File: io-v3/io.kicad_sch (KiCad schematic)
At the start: 99 parts, among them P1 OUT_GND, P10 INJ-CPU, P11 INJECTORS, P12 LSD-CPU, P13 LSDS, P2 TRIG-cpu, P3 DIG-CPU, P4 IN-CPU, P5 CPU_PWR, P6 TRIG-IN, P7 DIG-IN, P8 IGNITION, P9 PWR_IN, Q1 MOSFET, Q2 MOSFET, Q3 MOSFET, Q4 MOSFET, Q5 MOSFET, Q6 MOSFET, Q7 MOSFET, Q8 MOSFET, U1 LM2940, U12 MIC4469, U13 MIC4469, U2 MIC4469, U3 MAX9926UAEE+

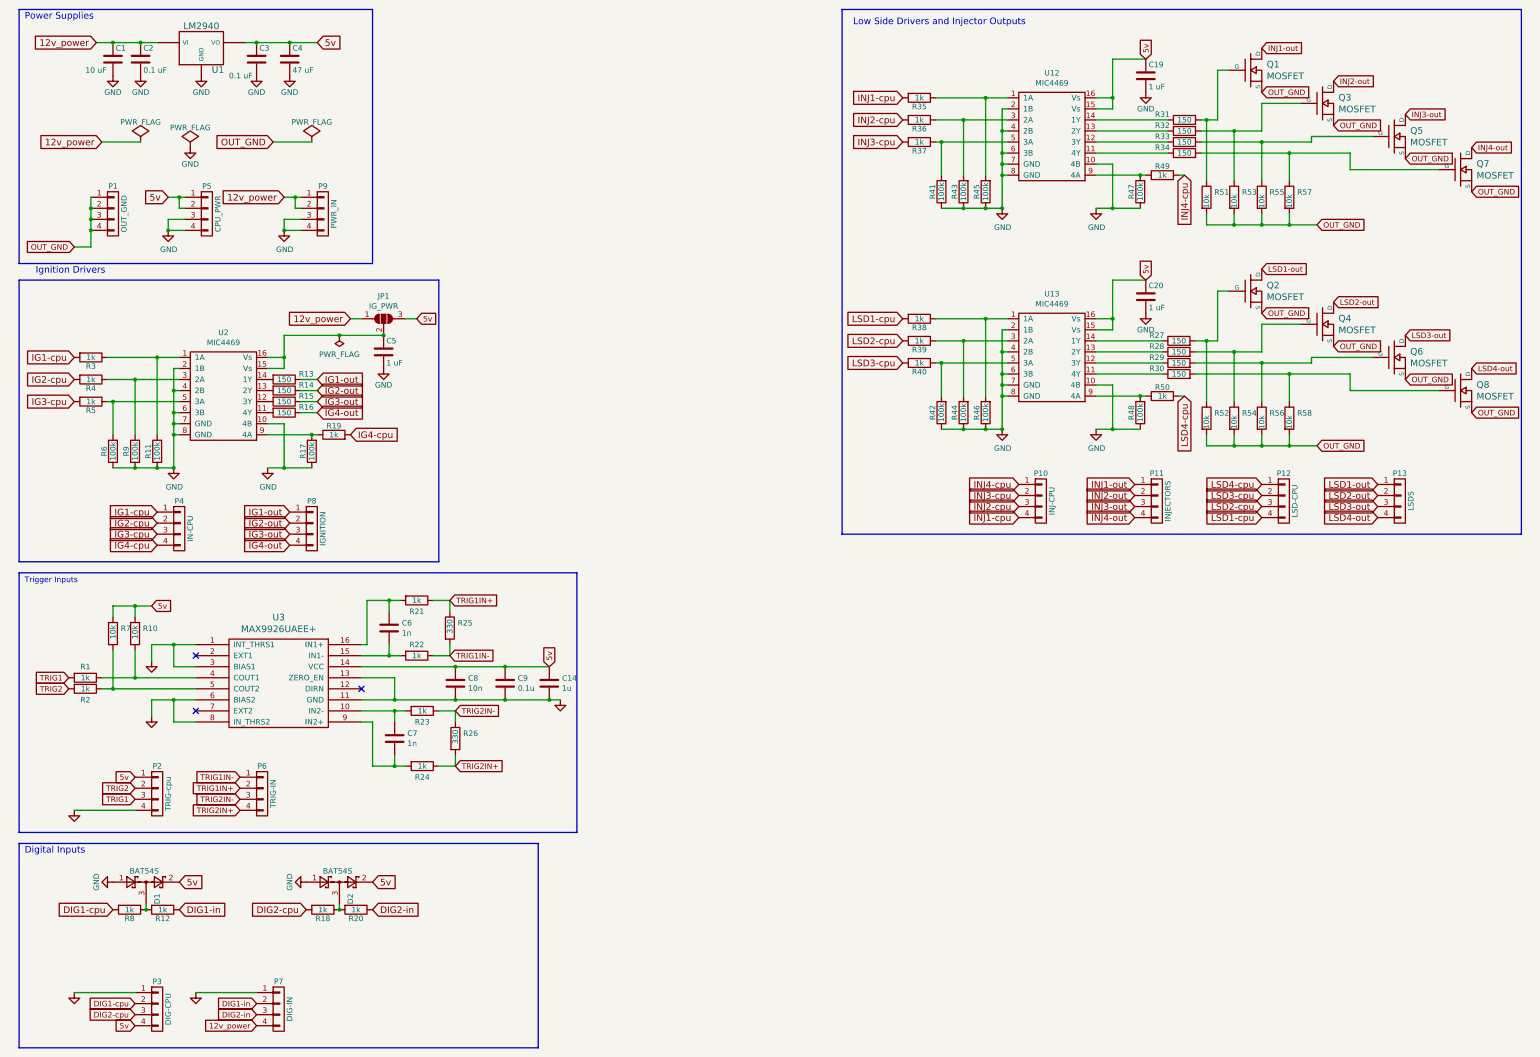
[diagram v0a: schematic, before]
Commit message: Add LEDs and make a board size
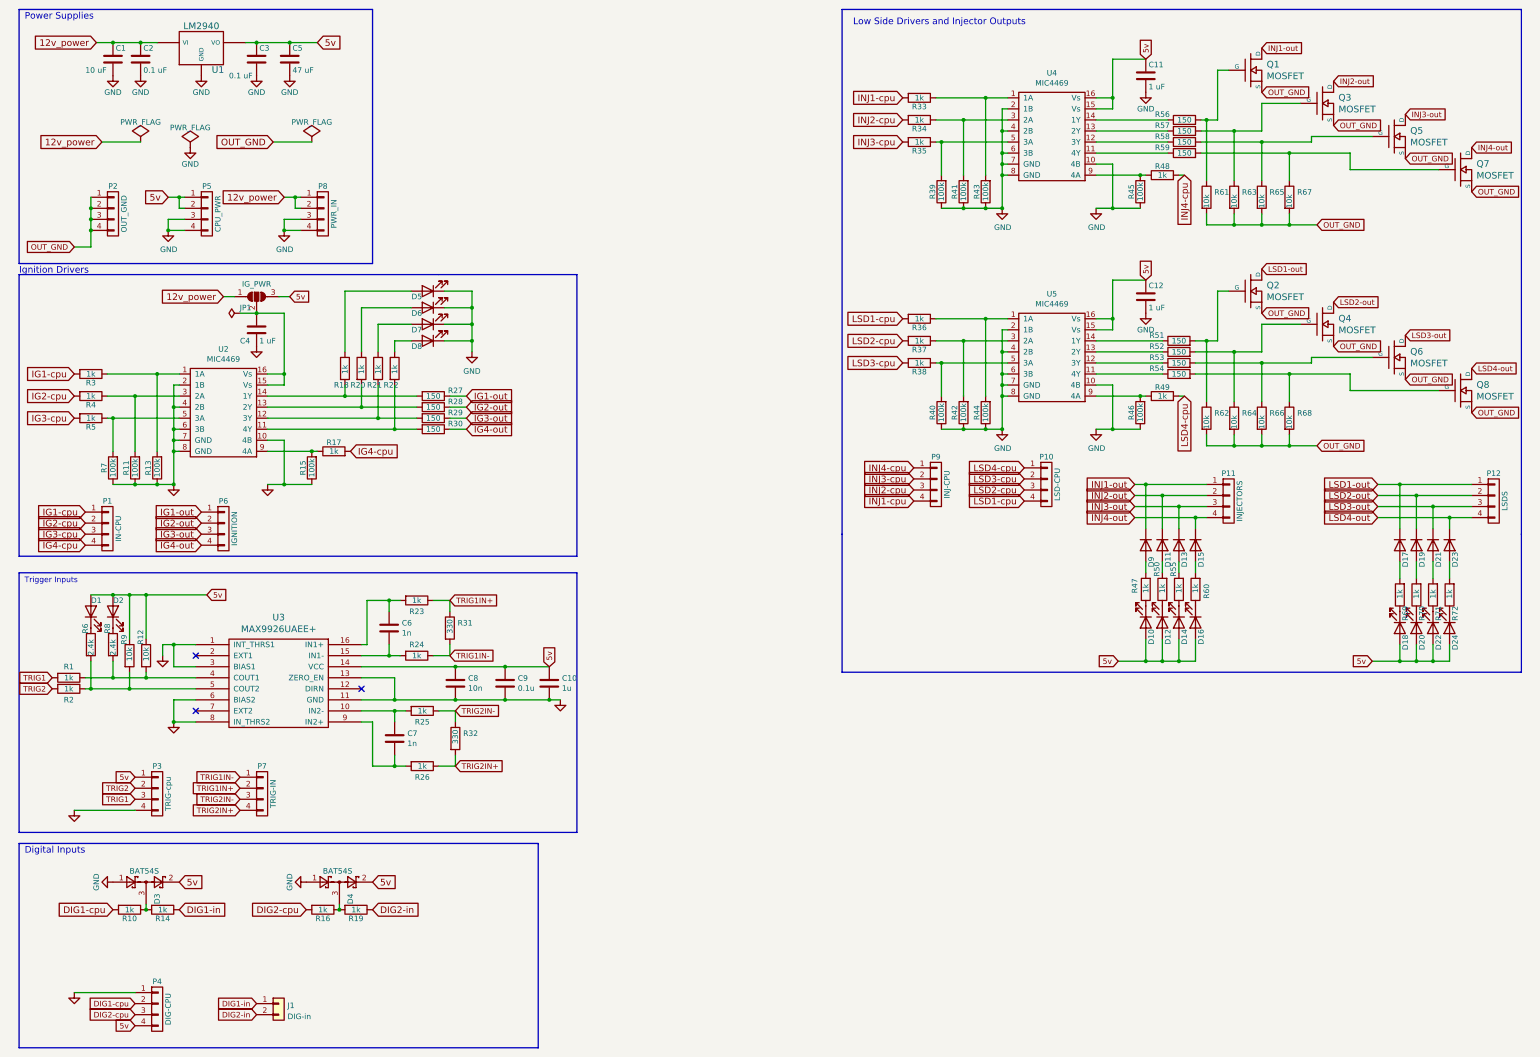
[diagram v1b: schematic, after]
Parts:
- removed P7: DIG-IN, Connector_PinHeader_2.54mm:PinHeader_1x04_P2.54mm_Vertical, symbol io-rescue:CONN_01X04-io-rescue-io-rescue
- added D1, D10, D12, D14, D16, D18, D2, D20, D22, D24, D5, D6, D7, D8: LED, LED_SMD:LED_0805_2012Metric_Pad1.15x1.40mm_HandSolder, symbol Device:LED
- added D11, D13, D15, D17, D19, D21, D23, D9: 1N4148, Diode_SMD:D_0805_2012Metric_Pad1.15x1.40mm_HandSolder, symbol Diode:1N4148
- added J1: DIG-in, Connector_PinHeader_2.54mm:PinHeader_1x02_P2.54mm_Vertical, symbol Connector_Generic:Conn_01x02
- added R18, R20, R21, R22, R47, R50, R55, R60, R69, R70, R71, R72: 1k, Resistor_SMD:R_0805_2012Metric_Pad1.20x1.40mm_HandSolder, symbol Device:R
- added R6, R8: 2.4k, Resistor_SMD:R_0805_2012Metric_Pad1.20x1.40mm_HandSolder, symbol Device:R
- renumbered C14 to C10, C19 to C11, C20 to C12, C5 to C4, C4 to C5, D1 to D3, D2 to D4, P4 to P1, P12 to P10, P13 to P12, P1 to P2, P2 to P3, P3 to P4, P8 to P6, P6 to P7, P9 to P8, P10 to P9, R8 to R10, R9 to R11, R10 to R12, R11 to R13, R12 to R14, R17 to R15, R18 to R16, R19 to R17, R20 to R19, R21 to R23, R22 to R24, R23 to R25, R24 to R26, R13 to R27, R14 to R28, R15 to R29, R16 to R30, R25 to R31, R26 to R32, R35 to R33, R36 to R34, R37 to R35, R38 to R36, R39 to R37, R40 to R38, R41 to R39, R42 to R40, R43 to R41, R44 to R42, R45 to R43, R46 to R44, R47 to R45, R48 to R46, R49 to R48, R50 to R49, R27 to R51, R28 to R52, R29 to R53, R30 to R54, R31 to R56, R32 to R57, R33 to R58, R34 to R59, R51 to R61, R52 to R62, R53 to R63, R54 to R64, R55 to R65, R56 to R66, R57 to R67, R58 to R68, R6 to R7, R7 to R9, U12 to U4, U13 to U5
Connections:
- net 5v: now also D1.2 (A), D10.2 (A), D12.2 (A), D14.2 (A), D16.2 (A), D18.2 (A), D2.2 (A), D20.2 (A), D22.2 (A), D24.2 (A)
- net DIG1-in: now also J1.1 (Pin_1)
- net DIG2-in: now also J1.2 (Pin_2)
- net GND: now also D5.1 (K), D6.1 (K), D7.1 (K), D8.1 (K)
- net INJ1-out: now also D9.1 (K)
- net INJ2-out: now also D11.1 (K)
- net INJ3-out: now also D13.1 (K)
- net INJ4-out: now also D15.1 (K)
- net LSD1-out: now also D17.1 (K)
- net LSD2-out: now also D19.1 (K)
- net LSD3-out: now also D21.1 (K)
- net LSD4-out: now also D23.1 (K)
- net at R27.2, U2.14 (1Y): now also R18.2
- net at R30.2, U2.11 (4Y): now also R22.2
- net at R29.2, U2.12 (3Y): now also R21.2
- net at R28.2, U2.13 (2Y): now also R20.2
- net at R1.1, R12.2, U3.4 (COUT1): now also R8.2
- net at R2.1, R9.2, U3.5 (COUT2): now also R6.2
- new net: D11.2 (A), R50.2
- new net: D20.1 (K), R70.1
- new net: D19.2 (A), R70.2
- new net: D22.1 (K), R71.1
- new net: D14.1 (K), R55.1
- new net: D18.1 (K), R69.1
- new net: D17.2 (A), R69.2
- new net: D21.2 (A), R71.2
- new net: D12.1 (K), R50.1
- new net: D2.1 (K), R8.1
- new net: D24.1 (K), R72.1
- new net: D23.2 (A), R72.2
- new net: D10.1 (K), R47.1
- new net: D7.2 (A), R21.1
- new net: D9.2 (A), R47.2
- new net: D8.2 (A), R22.1
- new net: D5.2 (A), R18.1
- new net: D6.2 (A), R20.1
- new net: D15.2 (A), R60.2
- new net: D16.1 (K), R60.1
- new net: D1.1 (K), R6.1
- new net: D13.2 (A), R55.2
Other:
- moved on the sheet: C4, JP1, P1, P10, P11, P12, P6, P9, R1, R11, R12, R13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

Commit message: Rework IO board to just be an LSD breakout board
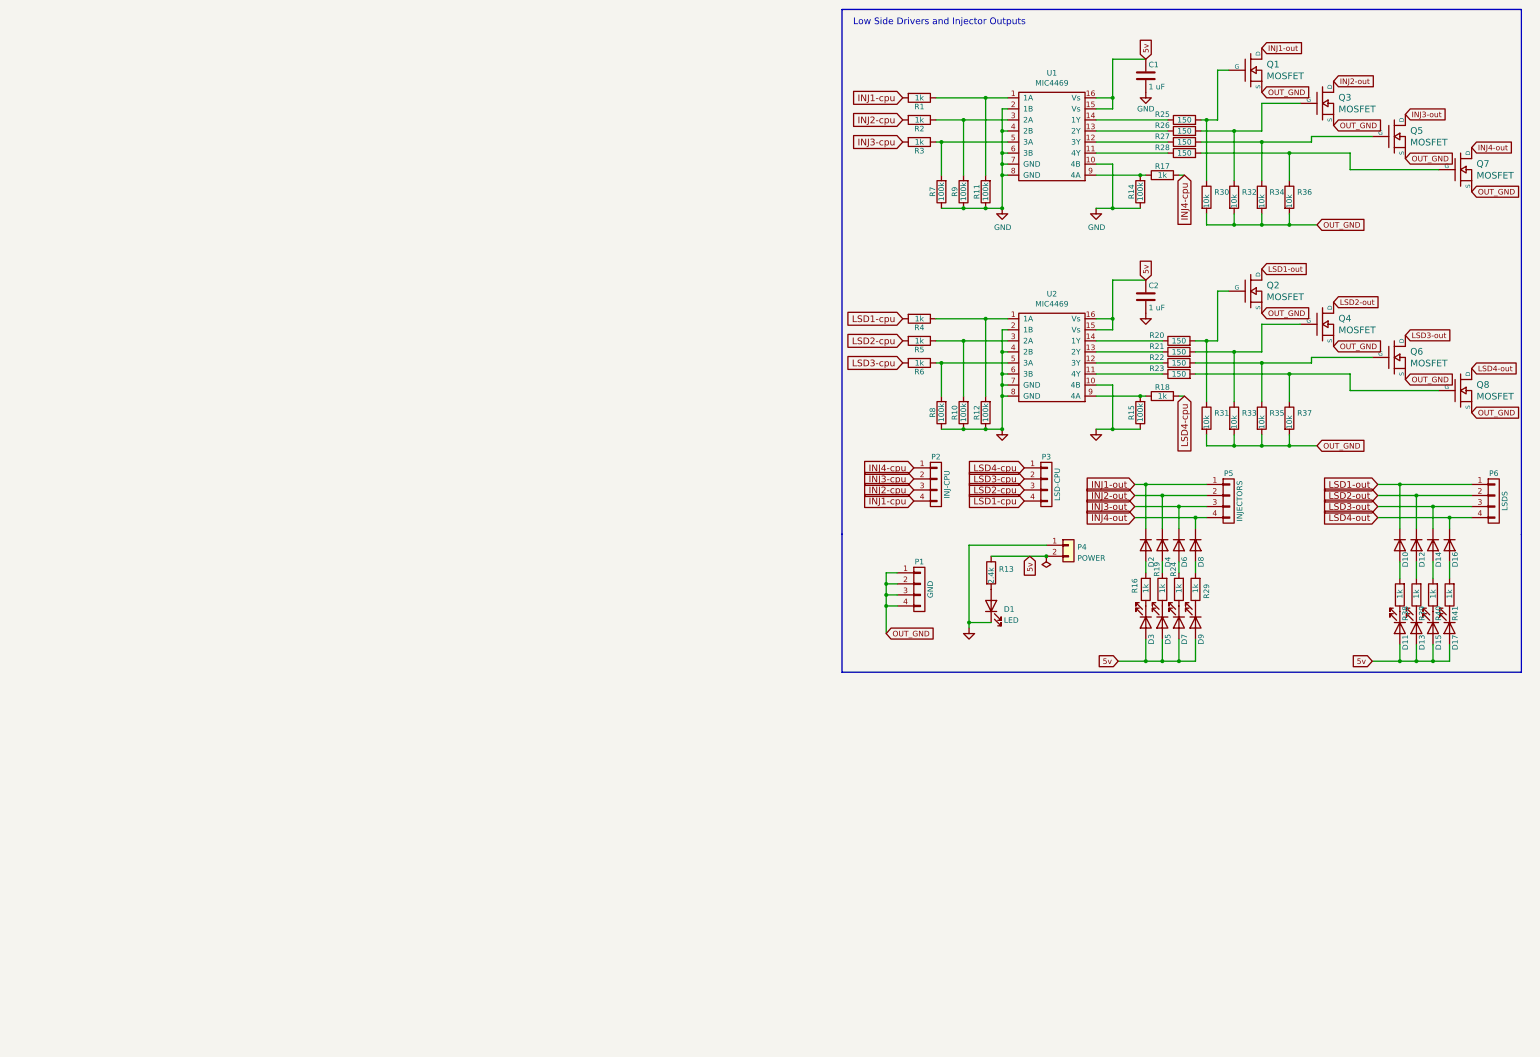
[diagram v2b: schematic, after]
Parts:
- removed C1: 10 uF, Capacitor_SMD:C_0805_2012Metric_Pad1.18x1.45mm_HandSolder, symbol io-rescue:C-io-rescue-io-rescue
- removed C10: 1u, Capacitor_SMD:C_0805_2012Metric_Pad1.18x1.45mm_HandSolder, symbol io-rescue:C-analog-rescue
- removed C2, C3: 0.1 uF, Capacitor_SMD:C_0805_2012Metric_Pad1.18x1.45mm_HandSolder, symbol io-rescue:C-io-rescue-io-rescue
- removed C4: 1 uF, Capacitor_SMD:C_0805_2012Metric_Pad1.18x1.45mm_HandSolder, symbol io-rescue:C-io-rescue-io-rescue
- removed C5: 47 uF, Capacitor_SMD:C_1206_3216Metric, symbol io-rescue:C-io-rescue-io-rescue
- removed C6, C7: 1n, Capacitor_SMD:C_0805_2012Metric_Pad1.18x1.45mm_HandSolder, symbol io-rescue:C-analog-rescue
- removed C8: 10n, Capacitor_SMD:C_0805_2012Metric_Pad1.18x1.45mm_HandSolder, symbol io-rescue:C-analog-rescue
- removed C9: 0.1u, Capacitor_SMD:C_0805_2012Metric_Pad1.18x1.45mm_HandSolder, symbol io-rescue:C-analog-rescue
- removed D2, D5, D6, D7, D8: LED, LED_SMD:LED_0805_2012Metric_Pad1.15x1.40mm_HandSolder, symbol Device:LED
- removed D3, D4: BAT54S, Package_TO_SOT_SMD:SOT-23, symbol Diode:BAT54S
- removed J1: DIG-in, Connector_PinHeader_2.54mm:PinHeader_1x02_P2.54mm_Vertical, symbol Connector_Generic:Conn_01x02
- removed JP1: IG_PWR, Jumper:SolderJumper-3_P1.3mm_Open_Pad1.0x1.5mm, symbol io-rescue:SolderJumper_3_Open-Jumper
- removed P2: OUT_GND, Connector_PinHeader_2.54mm:PinHeader_1x04_P2.54mm_Vertical, symbol io-rescue:CONN_01X04-io-rescue-io-rescue
- removed P3: TRIG-cpu, Connector_PinHeader_2.54mm:PinHeader_1x04_P2.54mm_Vertical, symbol io-rescue:CONN_01X04-io-rescue-io-rescue
- removed P4: DIG-CPU, Connector_PinHeader_2.54mm:PinHeader_1x04_P2.54mm_Vertical, symbol io-rescue:CONN_01X04-io-rescue-io-rescue
- removed P5: CPU_PWR, Connector_PinHeader_2.54mm:PinHeader_1x04_P2.54mm_Vertical, symbol io-rescue:CONN_01X04-io-rescue-io-rescue
- removed P6: IGNITION, Connector_PinHeader_2.54mm:PinHeader_1x04_P2.54mm_Vertical, symbol io-rescue:CONN_01X04-io-rescue-io-rescue
- removed P7: TRIG-IN, Connector_PinHeader_2.54mm:PinHeader_1x04_P2.54mm_Vertical, symbol io-rescue:CONN_01X04-io-rescue-io-rescue
- removed P8: PWR_IN, Connector_PinHeader_2.54mm:PinHeader_1x04_P2.54mm_Vertical, symbol io-rescue:CONN_01X04-io-rescue-io-rescue
- removed R1, R2, R23, R24, R25, R26: 1k, Resistor_SMD:R_0805_2012Metric_Pad1.20x1.40mm_HandSolder, symbol io-rescue:R-analog-rescue
- removed R10, R14, R16, R17, R19, R3, R4, R5: 1k, Resistor_SMD:R_0805_2012Metric_Pad1.20x1.40mm_HandSolder, symbol io-rescue:R-io-rescue-io-rescue
- removed R11, R13, R15, R7: 100k, Resistor_SMD:R_0805_2012Metric_Pad1.20x1.40mm_HandSolder, symbol io-rescue:R-io-rescue-io-rescue
- removed R12, R9: 10k, Resistor_SMD:R_0805_2012Metric_Pad1.20x1.40mm_HandSolder, symbol io-rescue:R-analog-rescue
- removed R18, R20, R21, R22: 1k, Resistor_SMD:R_0805_2012Metric_Pad1.20x1.40mm_HandSolder, symbol Device:R
- removed R27, R28, R29, R30: 150, Resistor_SMD:R_0805_2012Metric_Pad1.20x1.40mm_HandSolder, symbol io-rescue:R-io-rescue-io-rescue
- removed R31, R32: 330, Resistor_THT:R_Axial_DIN0207_L6.3mm_D2.5mm_P2.54mm_Vertical, symbol io-rescue:R-analog-rescue
- removed R6, R8: 2.4k, Resistor_SMD:R_0805_2012Metric_Pad1.20x1.40mm_HandSolder, symbol Device:R
- removed U1: LM2940, Package_TO_SOT_THT:TO-220-3_Horizontal_TabDown, symbol io-rescue:LM2940-io-rescue-io-rescue
- removed U2: MIC4469, Package_SO:SOIC-16W_7.5x10.3mm_P1.27mm, symbol io-rescue:MIC4469-viaems-io-rescue
- removed U3: MAX9926UAEE+, Package_SO:QSOP-16_3.9x4.9mm_P0.635mm, symbol io-rescue:MAX9926UAEE+-viaems
- added P4: POWER, Connector_PinHeader_2.54mm:PinHeader_1x02_P2.54mm_Vertical, symbol Connector_Generic:Conn_01x02
- added R13: 2.4k, Resistor_SMD:R_0805_2012Metric_Pad1.20x1.40mm_HandSolder, symbol Device:R
- D1: footprint LED_SMD:LED_0805_2012Metric_Pad1.15x1.40mm_HandSolder -> LED_SMD:LED_0805_2012Metric
- P1: value IN-CPU -> GND; footprint Connector_PinHeader_2.54mm:PinHeader_1x04_P2.54mm_Vertical -> Connector_PinHeader_2.54mm:PinHeader_2x02_P2.54mm_Vertical
- renumbered C11 to C1, C12 to C2, D17 to D10, D18 to D11, D19 to D12, D20 to D13, D21 to D14, D22 to D15, D23 to D16, D24 to D17, D9 to D2, D10 to D3, D11 to D4, D12 to D5, D13 to D6, D14 to D7, D15 to D8, D16 to D9, P9 to P2, P10 to P3, P11 to P5, P12 to P6, R33 to R1, R42 to R10, R43 to R11, R44 to R12, R45 to R14, R46 to R15, R47 to R16, R48 to R17, R49 to R18, R50 to R19, R34 to R2, R51 to R20, R52 to R21, R53 to R22, R54 to R23, R55 to R24, R56 to R25, R57 to R26, R58 to R27, R59 to R28, R60 to R29, R35 to R3, R61 to R30, R62 to R31, R63 to R32, R64 to R33, R65 to R34, R66 to R35, R67 to R36, R68 to R37, R69 to R38, R70 to R39, R36 to R4, R71 to R40, R72 to R41, R37 to R5, R38 to R6, R39 to R7, R40 to R8, R41 to R9, U4 to U1, U5 to U2
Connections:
- net IG1-cpu is gone; now on net OUT_GND: P1.1 (P1)
- net IG2-cpu is gone; now on net OUT_GND: P1.2 (P2)
- net IG3-cpu is gone; now on net OUT_GND: P1.3 (P3)
- net IG4-cpu is gone; now on net OUT_GND: P1.4 (P4)
- net 5v: now also P4.2 (Pin_2), R13.1; no longer D1.2 (A)
- net GND: now also D1.1 (K), P4.1 (Pin_1)
- new net: D1.2 (A), R13.2
- no-connect marks 3 -> 0
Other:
- note removed: "Digital Inputs"
- note removed: "Ignition Drivers"
- note removed: "Power Supplies"
- note removed: "Trigger Inputs"
